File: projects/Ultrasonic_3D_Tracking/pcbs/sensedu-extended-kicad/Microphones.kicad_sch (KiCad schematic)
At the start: 40 parts, among them J14 Conn_02x01, U1 AD8426ACPZ-R7, U2 AD8426ACPZ-R7, U3 LT1790ACS6-1.25

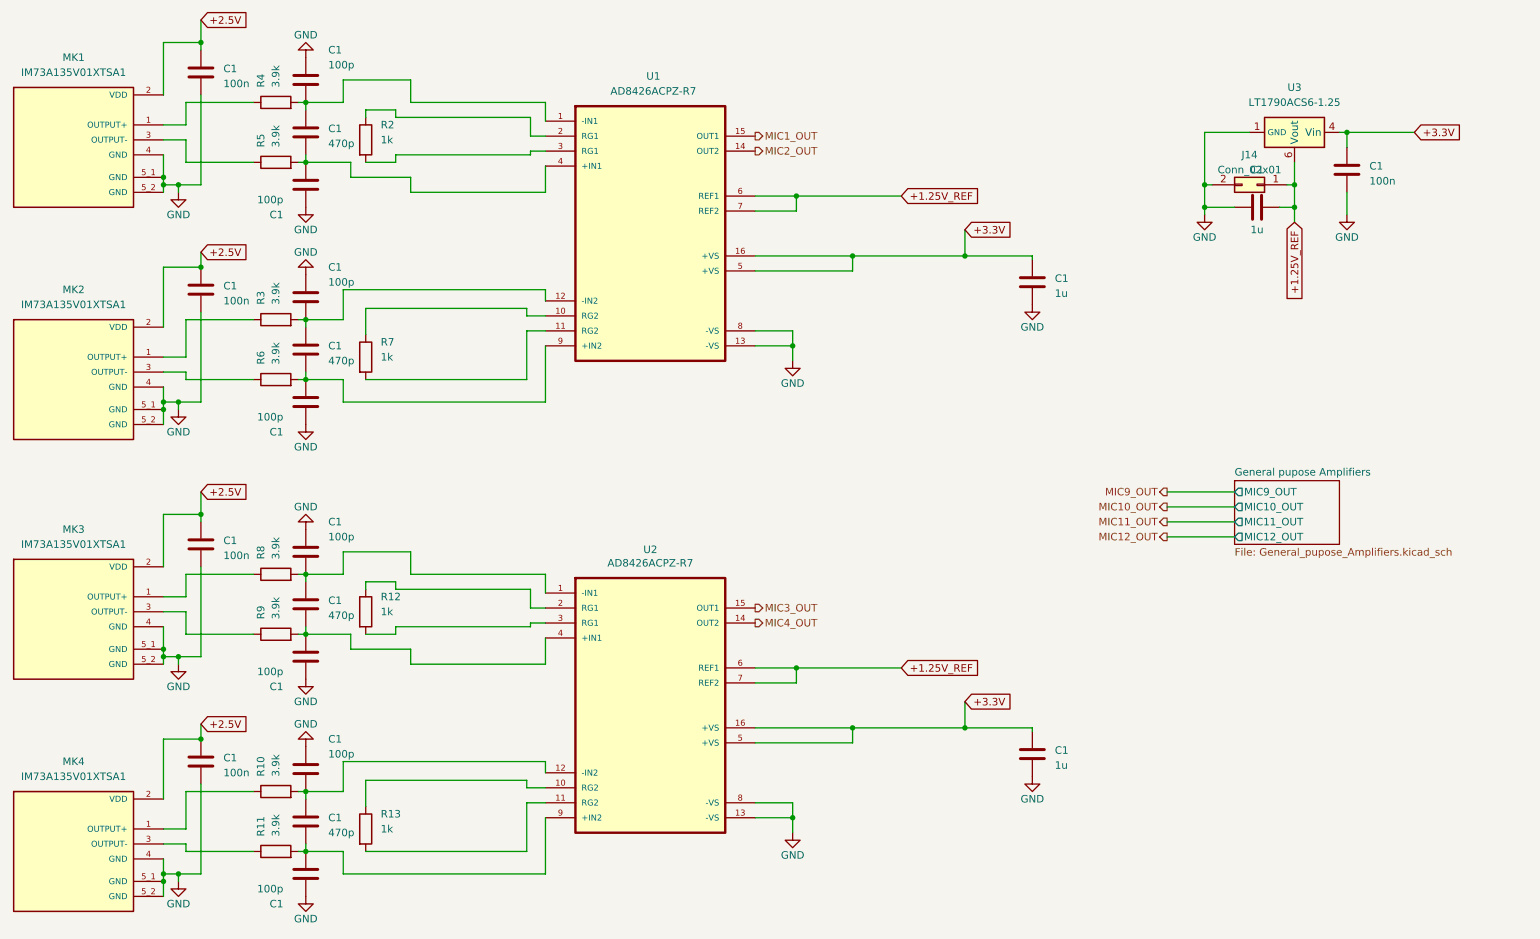
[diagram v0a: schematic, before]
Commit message: Fix: Cleaned schematic
- project is not correctly set up, so cannot be ordered without further
   work
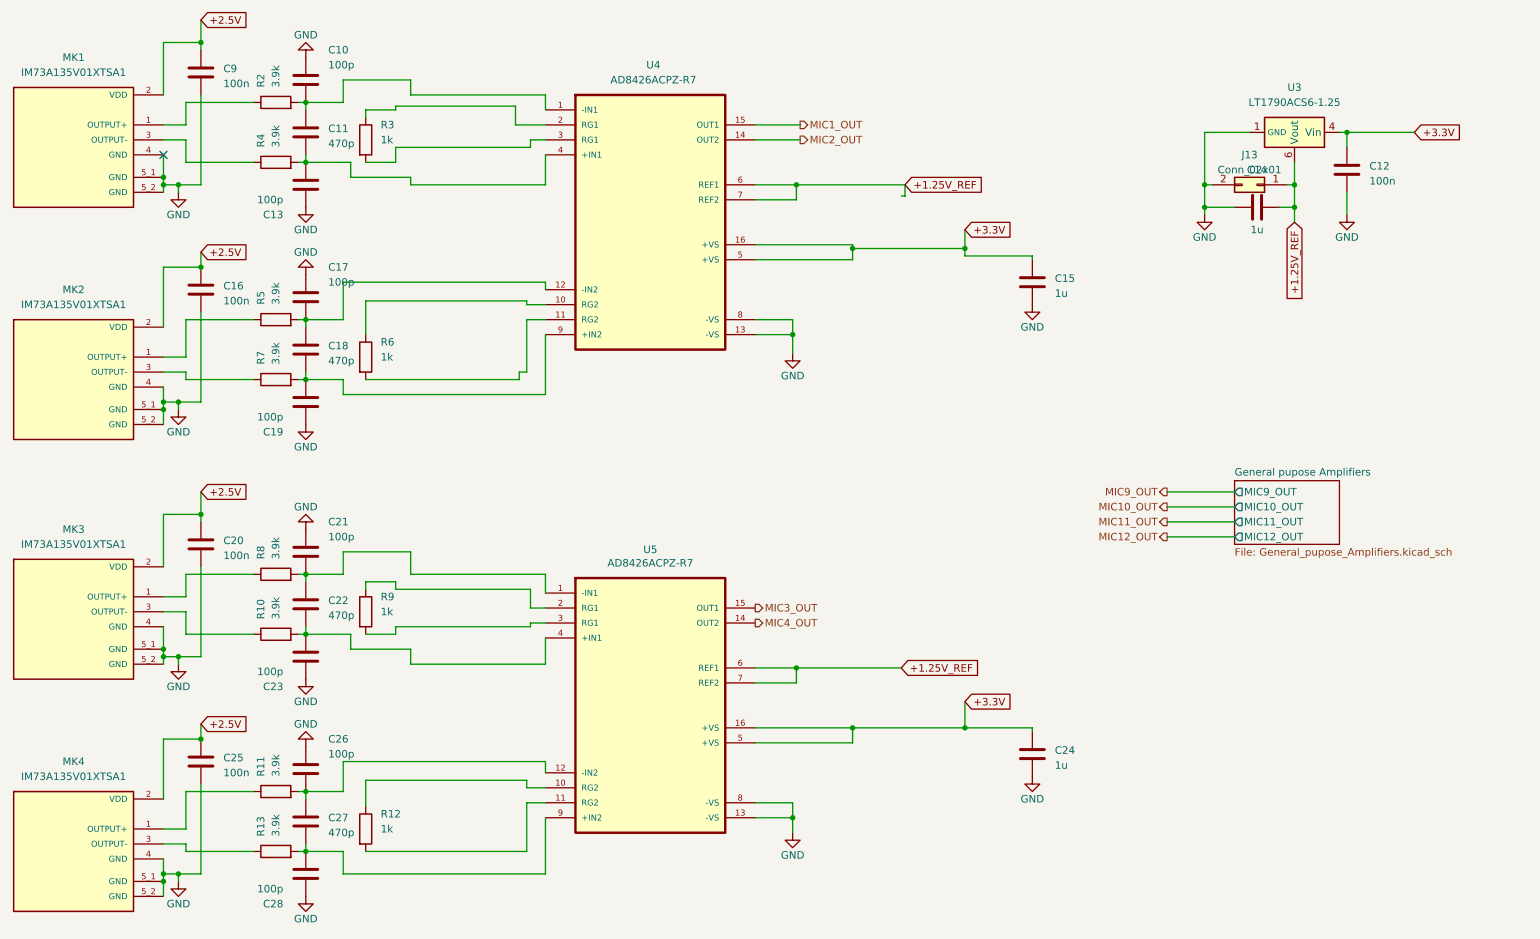
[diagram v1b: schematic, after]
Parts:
- renumbered C1 to C10, C1 to C11, C1 to C12, C1 to C13, C1 to C14, C1 to C15, C1 to C16, C1 to C17, C1 to C18, C1 to C19, C1 to C20, C1 to C21, C1 to C22, C1 to C23, C1 to C24, C1 to C25, C1 to C26, C1 to C27, C1 to C28, C1 to C9, J14 to J13, R9 to R10, R10 to R11, R13 to R12, R11 to R13, R4 to R2, R2 to R3, R5 to R4, R3 to R5, R7 to R6, R6 to R7, R12 to R9, U1 to U4, U2 to U5
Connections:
- no-connect marks 0 -> 1
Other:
- moved on the sheet: U4
